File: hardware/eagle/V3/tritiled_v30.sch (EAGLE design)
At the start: 12 parts, among them IC1 PIC12LF1571

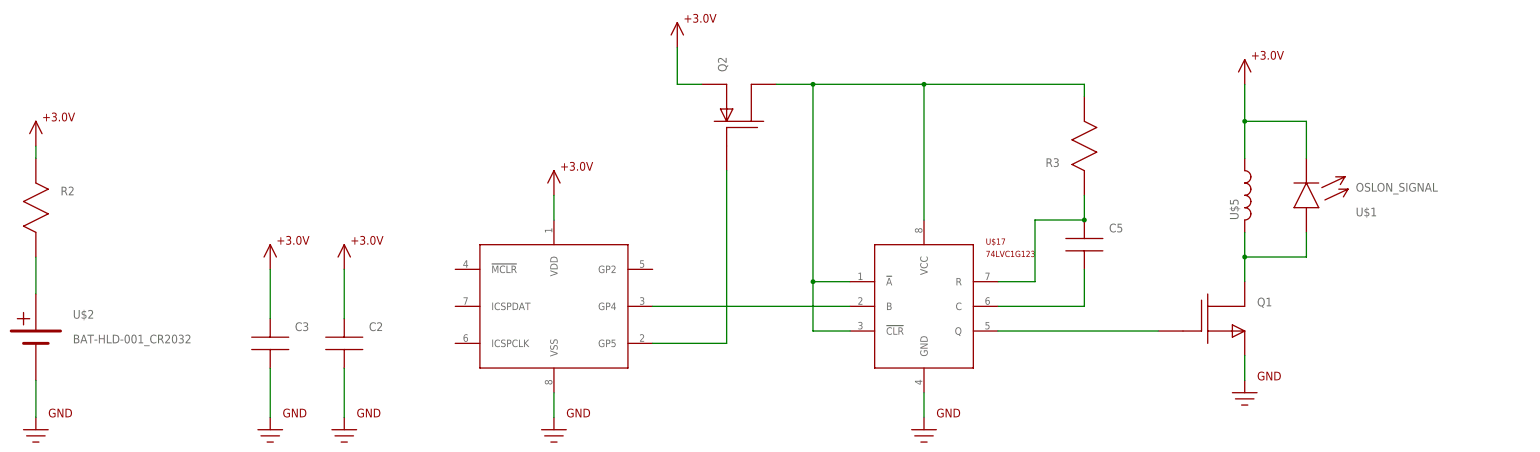
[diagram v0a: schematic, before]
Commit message: Fixed V3.0 board (74LVC1G123 A_bar now pulled low)
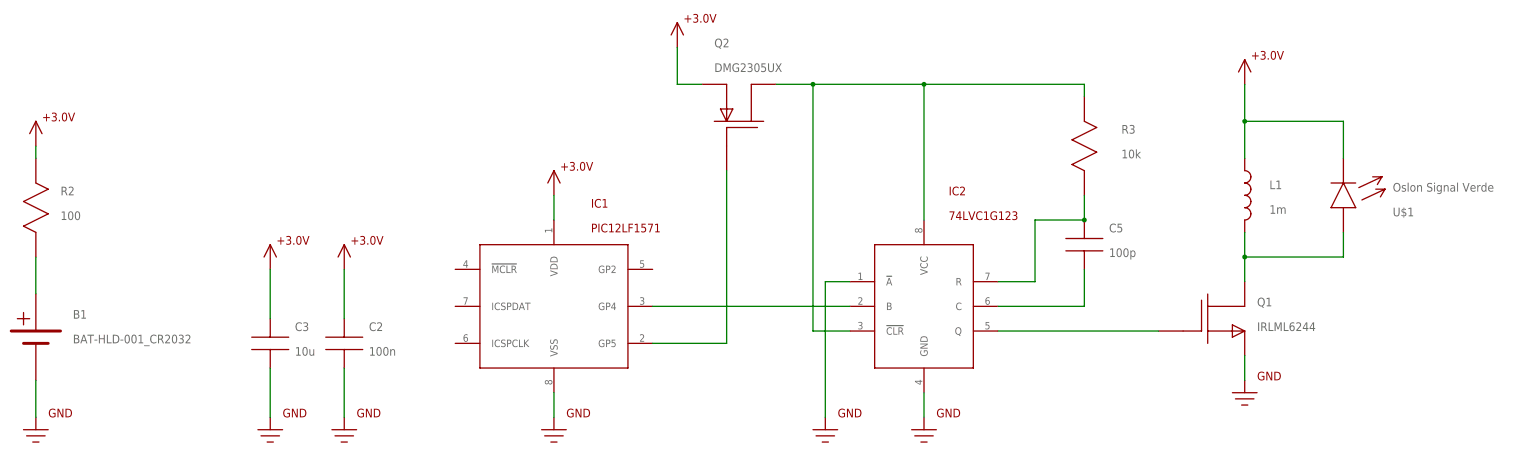
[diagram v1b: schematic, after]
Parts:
- C2: value (none) -> 100n
- C3: value (none) -> 10u
- C5: value (none) -> 100p
- L1: value (none) -> 1m
- Q1: value (none) -> IRLML6244
- Q2: value (none) -> DMG2305UX
- R2: value (none) -> 100
- R3: value (none) -> 10k
- U$1: value OSLON_SIGNAL -> Oslon Signal Verde
- renumbered U$17 to IC2, U$2 to B1, U$5 to L1
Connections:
- net GND: now also IC2.!A!
- net N$7: no longer IC2.!A!
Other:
- moved on the sheet: U$1
